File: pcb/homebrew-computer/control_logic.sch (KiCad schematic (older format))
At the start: 24 parts

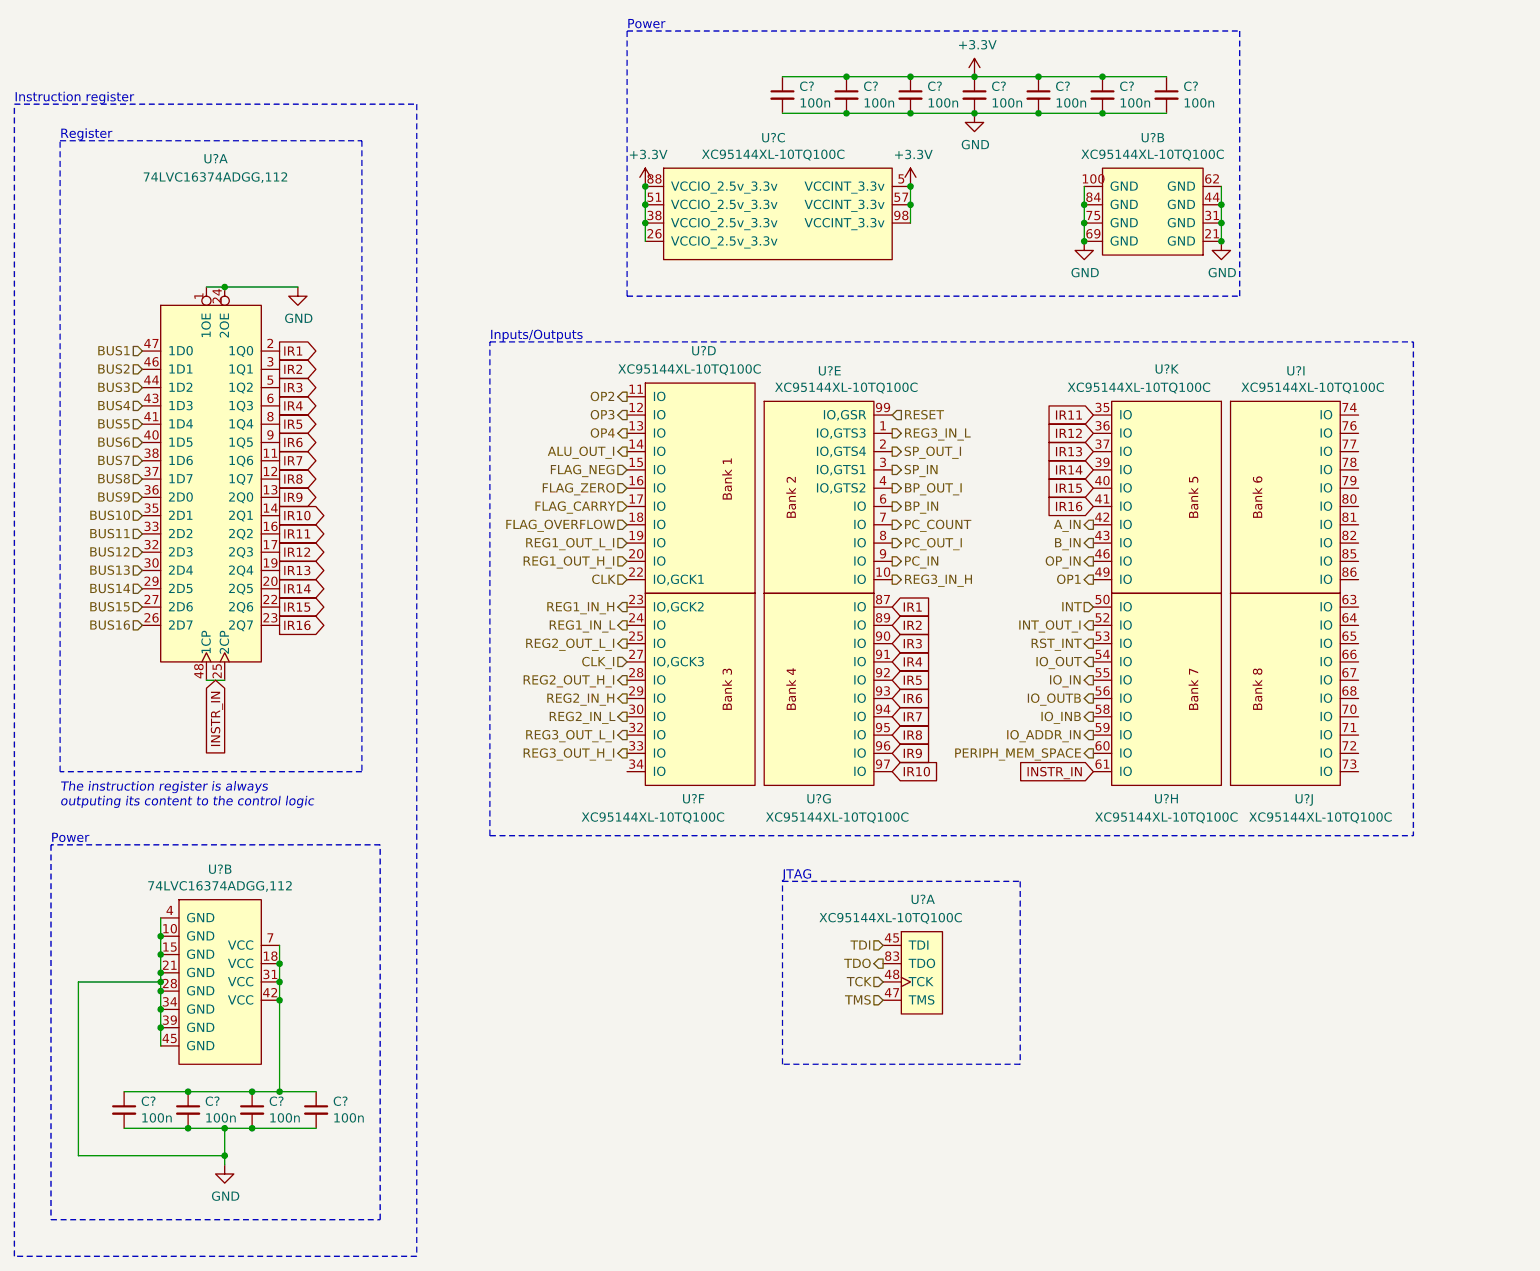
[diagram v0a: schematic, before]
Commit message: Start changing global labels with local labels
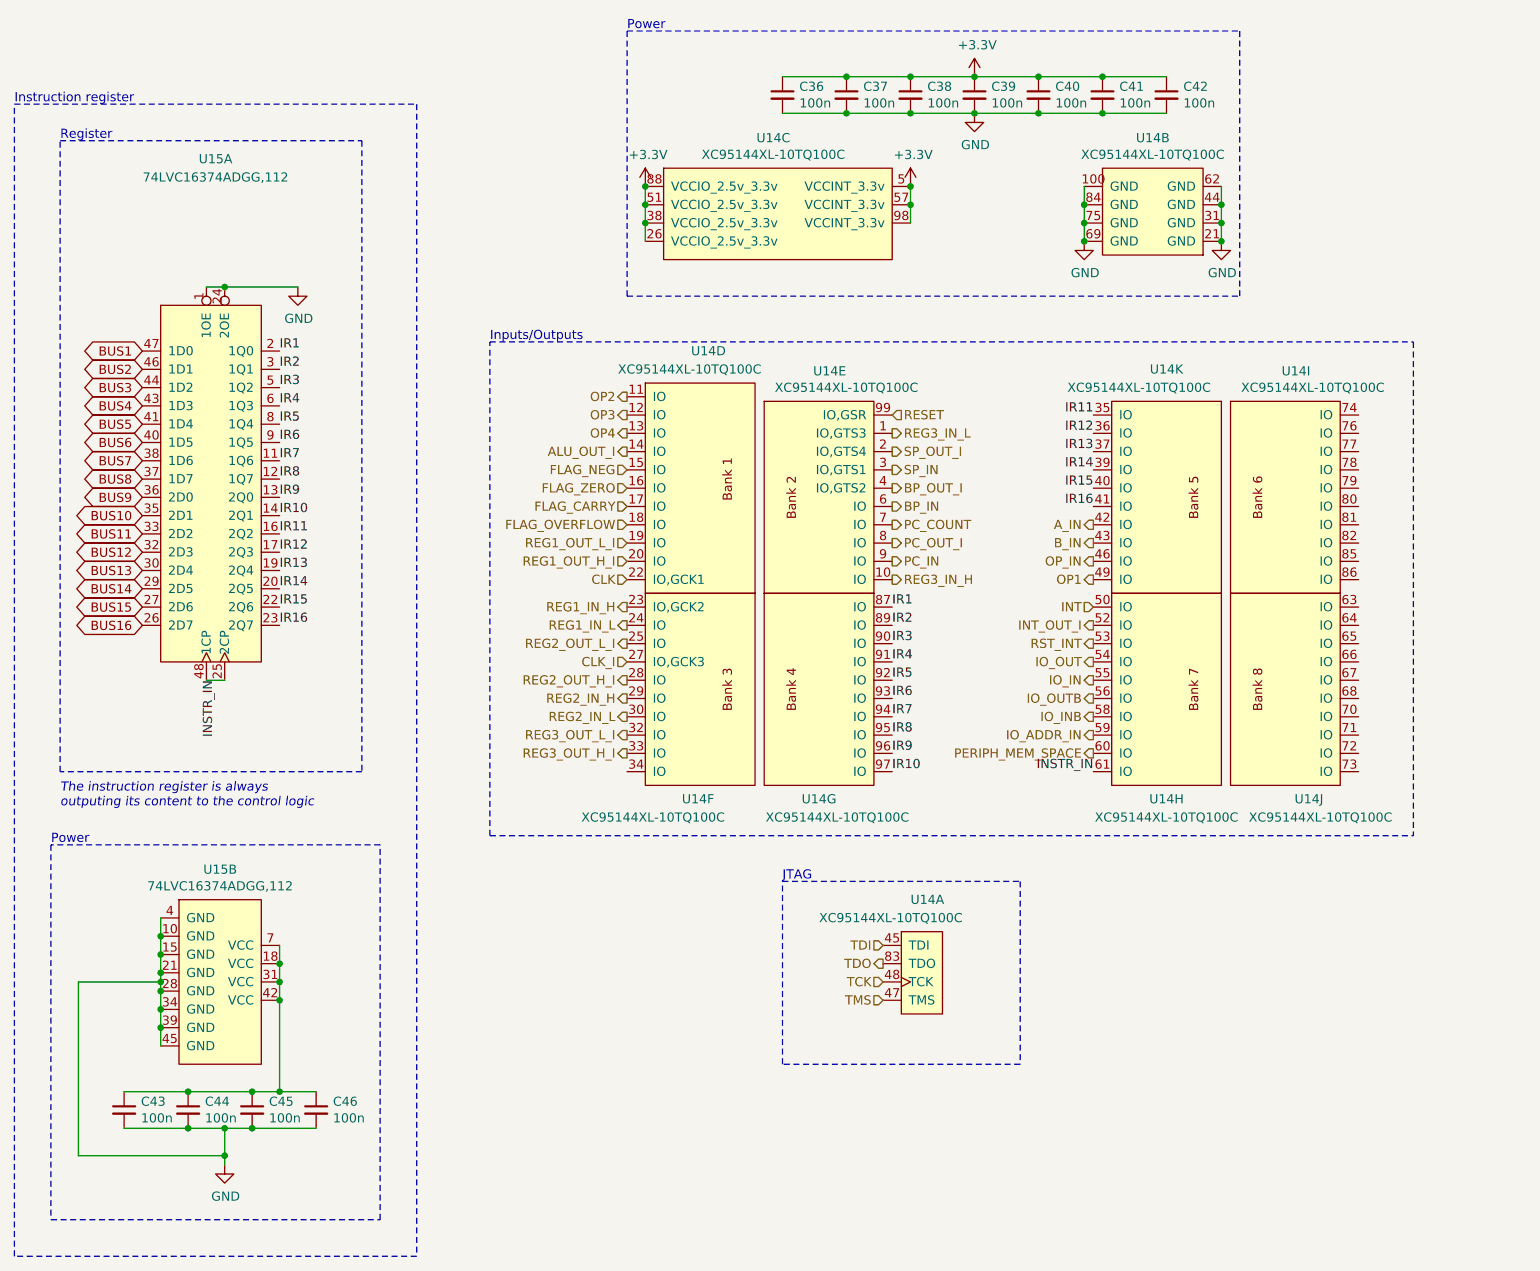
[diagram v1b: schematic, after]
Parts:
- gave numbers to parts that had none: 13

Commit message: Start working on the pcb layout
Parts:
- C36, C37, C38, C39, C40, C41, C42, C43, C44, C45, C46: footprint (none) -> Capacitor_SMD:C_0402_1005Metric_Pad0.74x0.62mm_HandSolder
- U14: footprint (none) -> Package_QFP:TQFP-100_14x14mm_P0.5mm
- U15: footprint (none) -> Package_SO:TSSOP-48_6.1x12.5mm_P0.5mm
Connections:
- net +3V3: now also C43.1, C44.1, C45.1, C46.1, U15.18 (VCC), U15.31 (VCC), U15.42 (VCC), U15.7 (VCC)
- no-connect marks 0 -> 21
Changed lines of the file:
@@
 F 0 "C39" H 6342 1046 50  0000 L CNN
 F 1 "100n" H 6342 955 50  0000 L CNN
-F 2 "" H 6250 1000 50  0001 C CNN
+F 2 "Capacitor_SMD:C_0402_1005Metric_Pad0.74x0.62mm_HandSolder" H 6250 1000 50  0001 C CNN
 F 3 "~" H 6250 1000 50  0001 C CNN
 	1    6250 1000
@@
 F 0 "C40" H 6692 1046 50  0000 L CNN
 F 1 "100n" H 6692 955 50  0000 L CNN
-F 2 "" H 6600 1000 50  0001 C CNN
+F 2 "Capacitor_SMD:C_0402_1005Metric_Pad0.74x0.62mm_HandSolder" H 6600 1000 50  0001 C CNN
 F 3 "~" H 6600 1000 50  0001 C CNN
 	1    6600 1000
@@
 F 0 "C41" H 7042 1046 50  0000 L CNN
 F 1 "100n" H 7042 955 50  0000 L CNN
-F 2 "" H 6950 1000 50  0001 C CNN
+F 2 "Capacitor_SMD:C_0402_1005Metric_Pad0.74x0.62mm_HandSolder" H 6950 1000 50  0001 C CNN
 F 3 "~" H 6950 1000 50  0001 C CNN
 	1    6950 1000
@@
 F 0 "U15" H 2100 2150 50  0000 C CNN
 F 1 "74LVC16374ADGG,112" H 2100 2050 50  0000 C CNN
-F 2 "" H 2100 1750 50  0001 C CNN
+F 2 "Package_SO:TSSOP-48_6.1x12.5mm_P0.5mm" H 2100 1750 50  0001 C CNN
 F 3 "" H 2100 1750 50  0001 C CNN
 	1    2100 1750
@@
 F 0 "U15" H 2125 5265 50  0000 C CNN
 F 1 "74LVC16374ADGG,112" H 2125 5174 50  0000 C CNN
-F 2 "" H 2100 5250 50  0001 C CNN
+F 2 "Package_SO:TSSOP-48_6.1x12.5mm_P0.5mm" H 2100 5250 50  0001 C CNN
 F 3 "" H 2100 5250 50  0001 C CNN
 	2    2100 5250
@@
 F 0 "C46" H 2742 6596 50  0000 L CNN
 F 1 "100n" H 2742 6505 50  0000 L CNN
-F 2 "" H 2650 6550 50  0001 C CNN
+F 2 "Capacitor_SMD:C_0402_1005Metric_Pad0.74x0.62mm_HandSolder" H 2650 6550 50  0001 C CNN
 F 3 "~" H 2650 6550 50  0001 C CNN
 	1    2650 6550
@@
 F 0 "C43" H 1692 6596 50  0000 L CNN
 F 1 "100n" H 1692 6505 50  0000 L CNN
-F 2 "" H 1600 6550 50  0001 C CNN
+F 2 "Capacitor_SMD:C_0402_1005Metric_Pad0.74x0.62mm_HandSolder" H 1600 6550 50  0001 C CNN
 F 3 "~" H 1600 6550 50  0001 C CNN
 	1    1600 6550
@@
 F 0 "C44" H 2042 6596 50  0000 L CNN
 F 1 "100n" H 2042 6505 50  0000 L CNN
-F 2 "" H 1950 6550 50  0001 C CNN
+F 2 "Capacitor_SMD:C_0402_1005Metric_Pad0.74x0.62mm_HandSolder" H 1950 6550 50  0001 C CNN
 F 3 "~" H 1950 6550 50  0001 C CNN
 	1    1950 6550
@@
 F 0 "C45" H 2392 6596 50  0000 L CNN
 F 1 "100n" H 2392 6505 50  0000 L CNN
-F 2 "" H 2300 6550 50  0001 C CNN
+F 2 "Capacitor_SMD:C_0402_1005Metric_Pad0.74x0.62mm_HandSolder" H 2300 6550 50  0001 C CNN
 F 3 "~" H 2300 6550 50  0001 C CNN
 	1    2300 6550
@@
 F 0 "U14" H 5900 5500 50  0000 L CNN
 F 1 "XC95144XL-10TQ100C" H 5400 5400 50  0000 L CNN
-F 2 "" H 5950 5450 50  0001 C CNN
+F 2 "Package_QFP:TQFP-100_14x14mm_P0.5mm" H 5950 5450 50  0001 C CNN
 F 3 "" H 5950 5450 50  0001 C CNN
 	1    5950 5450
@@
 F 0 "U14" H 7225 1365 50  0000 C CNN
 F 1 "XC95144XL-10TQ100C" H 7225 1274 50  0000 C CNN
-F 2 "" H 7200 1300 50  0001 C CNN
+F 2 "Package_QFP:TQFP-100_14x14mm_P0.5mm" H 7200 1300 50  0001 C CNN
 F 3 "" H 7200 1300 50  0001 C CNN
 	2    7200 1300
@@
 F 0 "U14" H 5150 1265 50  0000 C CNN
 F 1 "XC95144XL-10TQ100C" H 5150 1174 50  0000 C CNN
-F 2 "" H 5100 1250 50  0001 C CNN
+F 2 "Package_QFP:TQFP-100_14x14mm_P0.5mm" H 5100 1250 50  0001 C CNN
 F 3 "" H 5100 1250 50  0001 C CNN
 	3    5100 1250
@@
 F 0 "C36" H 5292 1046 50  0000 L CNN
 F 1 "100n" H 5292 955 50  0000 L CNN
-F 2 "" H 5200 1000 50  0001 C CNN
+F 2 "Capacitor_SMD:C_0402_1005Metric_Pad0.74x0.62mm_HandSolder" H 5200 1000 50  0001 C CNN
 F 3 "~" H 5200 1000 50  0001 C CNN
 	1    5200 1000
@@
 F 0 "C37" H 5642 1046 50  0000 L CNN
 F 1 "100n" H 5642 955 50  0000 L CNN
-F 2 "" H 5550 1000 50  0001 C CNN
+F 2 "Capacitor_SMD:C_0402_1005Metric_Pad0.74x0.62mm_HandSolder" H 5550 1000 50  0001 C CNN
 F 3 "~" H 5550 1000 50  0001 C CNN
 	1    5550 1000
@@
 F 0 "C38" H 5992 1046 50  0000 L CNN
 F 1 "100n" H 5992 955 50  0000 L CNN
-F 2 "" H 5900 1000 50  0001 C CNN
+F 2 "Capacitor_SMD:C_0402_1005Metric_Pad0.74x0.62mm_HandSolder" H 5900 1000 50  0001 C CNN
 F 3 "~" H 5900 1000 50  0001 C CNN
 	1    5900 1000
@@
 F 0 "C42" H 7392 1046 50  0000 L CNN
 F 1 "100n" H 7392 955 50  0000 L CNN
-F 2 "" H 7300 1000 50  0001 C CNN
+F 2 "Capacitor_SMD:C_0402_1005Metric_Pad0.74x0.62mm_HandSolder" H 7300 1000 50  0001 C CNN
 F 3 "~" H 7300 1000 50  0001 C CNN
 	1    7300 1000
@@
 F 0 "U14" H 4200 2400 50  0000 R CNN
 F 1 "XC95144XL-10TQ100C" H 4600 2300 50  0000 R CNN
-F 2 "" H 4450 2400 50  0001 C CNN
+F 2 "Package_QFP:TQFP-100_14x14mm_P0.5mm" H 4450 2400 50  0001 C CNN
 F 3 "" H 4450 2400 50  0001 C CNN
 	4    4450 2400
@@
 F 0 "U14" H 4650 2350 50  0000 R CNN
 F 1 "XC95144XL-10TQ100C" H 5200 2250 50  0000 R CNN
-F 2 "" H 4650 3600 50  0001 C CNN
+F 2 "Package_QFP:TQFP-100_14x14mm_P0.5mm" H 4650 3600 50  0001 C CNN
 F 3 "" H 4650 3600 50  0001 C CNN
 	6    4650 3600
@@
 F 0 "U14" H 7200 250 50  0000 C CNN
 F 1 "XC95144XL-10TQ100C" H 7200 150 50  0000 C CNN
-F 2 "" H 7250 2550 50  0001 C CNN
+F 2 "Package_QFP:TQFP-100_14x14mm_P0.5mm" H 7250 2550 50  0001 C CNN
 F 3 "" H 7250 2550 50  0001 C CNN
 	8    7250 2550
@@
 F 0 "U14" H 8008 2690 50  0000 C CNN
 F 1 "XC95144XL-10TQ100C" H 8100 2600 50  0000 C CNN
-F 2 "" H 7950 2575 50  0001 C CNN
+F 2 "Package_QFP:TQFP-100_14x14mm_P0.5mm" H 7950 2575 50  0001 C CNN
 F 3 "" H 7950 2575 50  0001 C CNN
 	9    7950 2600
@@
 F 0 "U14" H 6600 2350 50  0000 R CNN
 F 1 "XC95144XL-10TQ100C" H 6850 2250 50  0000 R CNN
-F 2 "" H 7300 3575 50  0001 C CNN
+F 2 "Package_QFP:TQFP-100_14x14mm_P0.5mm" H 7300 3575 50  0001 C CNN
 F 3 "" H 7300 3575 50  0001 C CNN
 	10   7300 3600
@@
 F 0 "U14" H 5458 2490 50  0000 C CNN
 F 1 "XC95144XL-10TQ100C" H 5550 2400 50  0000 C CNN
-F 2 "" H 5700 2475 50  0001 C CNN
+F 2 "Package_QFP:TQFP-100_14x14mm_P0.5mm" H 5700 2475 50  0001 C CNN
 F 3 "" H 5700 2475 50  0001 C CNN
 	5    5700 2500
@@
 F 0 "U14" H 5400 2350 50  0000 C CNN
 F 1 "XC95144XL-10TQ100C" H 5500 2250 50  0000 C CNN
-F 2 "" H 5500 3600 50  0001 C CNN
+F 2 "Package_QFP:TQFP-100_14x14mm_P0.5mm" H 5500 3600 50  0001 C CNN
 F 3 "" H 5500 3600 50  0001 C CNN
 	7    5500 3600
@@
 F 0 "U14" H 7300 4700 50  0000 C CNN
 F 1 "XC95144XL-10TQ100C" H 7150 4600 50  0000 C CNN
-F 2 "" H 7950 3575 50  0001 C CNN
+F 2 "Package_QFP:TQFP-100_14x14mm_P0.5mm" H 7950 3575 50  0001 C CNN
 F 3 "" H 7950 3575 50  0001 C CNN
 	11   7950 3600
@@
 Text Label 2100 4200 3    50   ~ 0
 INSTR_IN
+NoConn ~ 4350 4700
+NoConn ~ 8350 2750
+NoConn ~ 8350 2850
+NoConn ~ 8350 2950
+NoConn ~ 8350 3050
+NoConn ~ 8350 3150
+NoConn ~ 8350 3250
+NoConn ~ 8350 3350
+NoConn ~ 8350 3450
+NoConn ~ 8350 3550
+NoConn ~ 8350 3650
+NoConn ~ 8350 3800
+NoConn ~ 8350 3900
+NoConn ~ 8350 4000
+NoConn ~ 8350 4100
+NoConn ~ 8350 4200
+NoConn ~ 8350 4300
+NoConn ~ 8350 4400
+NoConn ~ 8350 4500
+NoConn ~ 8350 4600
+NoConn ~ 8350 4700
+$Comp
+L power:+3.3V #PWR?
+U 1 1 5FA740EC
+P 2450 5650
+AR Path="/5F8B5CB7/5FA740EC" Ref="#PWR?"  Part="1"
+AR Path="/5F95DC76/5FA740EC" Ref="#PWR?"  Part="1"
+AR Path="/5F8B5E3D/5FA740EC" Ref="#PWR0166"  Part="1"
+F 0 "#PWR0166" H 2450 5500 50  0001 C CNN
+F 1 "+3.3V" H 2600 5700 50  0000 C CNN
+F 2 "" H 2450 5650 50  0001 C CNN
+F 3 "" H 2450 5650 50  0001 C CNN
+	1    2450 5650
+	1    0    0    -1
+$EndComp
+Connection ~ 2450 5650
 $EndSCHEMATC

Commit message: Keep working on the layout
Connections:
- net A_IN: now also U14.89 (IO); no longer U14.42 (IO)
- net BP_IN: now also U14.32 (IO); no longer U14.6 (IO)
- net BP_OUT_I: now also U14.30 (IO); no longer U14.4 (IO,GTS2)
- net B_IN: now also U14.87 (IO); no longer U14.43 (IO)
- net FLAG_CARRY: now also U14.78 (IO); no longer U14.17 (IO)
- net FLAG_NEG: now also U14.77 (IO); no longer U14.15 (IO)
- net FLAG_OVERFLOW: now also U14.79 (IO); no longer U14.18 (IO)
- net FLAG_ZERO: now also U14.76 (IO); no longer U14.16 (IO)
- net INSTR_IN: now also U14.97 (IO); no longer U14.61 (IO)
- net IR1: now also U14.90 (IO); no longer U14.87 (IO)
- net IR10: now also U14.3 (IO,GTS1); no longer U14.97 (IO)
- net IR11: now also U14.4 (IO,GTS2); no longer U14.35 (IO)
- net IR12: now also U14.6 (IO); no longer U14.36 (IO)
- net IR13: now also U14.7 (IO); no longer U14.37 (IO)
- net IR14: now also U14.8 (IO); no longer U14.39 (IO)
- net IR15: now also U14.9 (IO); no longer U14.40 (IO)
- net IR16: now also U14.10 (IO); no longer U14.41 (IO)
- net IR2: now also U14.91 (IO); no longer U14.89 (IO)
- net IR3: now also U14.92 (IO); no longer U14.90 (IO)
- net IR4: now also U14.93 (IO); no longer U14.91 (IO)
- net IR5: now also U14.94 (IO); no longer U14.92 (IO)
- net IR6: now also U14.95 (IO); no longer U14.93 (IO)
- net IR7: now also U14.96 (IO); no longer U14.94 (IO)
- net IR8: now also U14.1 (IO,GTS3); no longer U14.95 (IO)
- net IR9: now also U14.2 (IO,GTS4); no longer U14.96 (IO)
- net OP1: now also U14.86 (IO); no longer U14.49 (IO)
- net OP2: now also U14.85 (IO); no longer U14.11 (IO)
- net OP3: now also U14.82 (IO); no longer U14.12 (IO)
- net OP4: now also U14.81 (IO); no longer U14.13 (IO)
- net OP_IN: now also U14.80 (IO); no longer U14.46 (IO)
- net PC_COUNT: now also U14.73 (IO); no longer U14.7 (IO)
- net PC_IN: now also U14.72 (IO); no longer U14.9 (IO)
- net PC_OUT_I: now also U14.74 (IO); no longer U14.8 (IO)
- net REG1_IN_H: now also U14.29 (IO); no longer U14.23 (IO,GCK2)
- net REG1_IN_L: no longer U14.24 (IO)
- net REG1_OUT_H_I: no longer U14.20 (IO)
- net REG1_OUT_L_I: no longer U14.19 (IO)
- net REG2_IN_H: no longer U14.29 (IO)
- net REG2_IN_L: no longer U14.30 (IO)
- net REG2_OUT_L_I: no longer U14.25 (IO)
- net REG3_IN_H: now also U14.41 (IO); no longer U14.10 (IO)
- net REG3_IN_L: now also U14.11 (IO); no longer U14.1 (IO,GTS3)
- net REG3_OUT_H_I: no longer U14.33 (IO)
- net REG3_OUT_L_I: no longer U14.32 (IO)
- net SP_IN: now also U14.34 (IO); no longer U14.3 (IO,GTS1)
- net SP_OUT_I: now also U14.33 (IO); no longer U14.2 (IO,GTS4)
- no-connect marks 21 -> 8
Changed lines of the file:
@@
 Wire Wire Line
 	2050 4200 2150 4200
-Text HLabel 6900 3350 0    50   Output ~ 0
+Text HLabel 5800 3900 2    50   Output ~ 0
 A_IN
-Text HLabel 6900 3450 0    50   Output ~ 0
+Text HLabel 5800 3800 2    50   Output ~ 0
 B_IN
-Text HLabel 6900 3550 0    50   Output ~ 0
+Text HLabel 8350 3250 2    50   Output ~ 0
 OP_IN
-Text HLabel 6900 3650 0    50   Output ~ 0
+Text HLabel 8350 3650 2    50   Output ~ 0
 OP1
-Text HLabel 4350 2650 0    50   Output ~ 0
+Text HLabel 8350 3550 2    50   Output ~ 0
 OP2
-Text HLabel 4350 2750 0    50   Output ~ 0
+Text HLabel 8350 3450 2    50   Output ~ 0
 OP3
-Text HLabel 4350 2850 0    50   Output ~ 0
+Text HLabel 8350 3350 2    50   Output ~ 0
 OP4
 Text HLabel 4350 2950 0    50   Output ~ 0
 ALU_OUT_I
-Text HLabel 4350 3050 0    50   Input ~ 0
+Text HLabel 8350 2950 2    50   Input ~ 0
 FLAG_NEG
-Text HLabel 4350 3150 0    50   Input ~ 0
+Text HLabel 8350 2850 2    50   Input ~ 0
 FLAG_ZERO
-Text HLabel 4350 3250 0    50   Input ~ 0
+Text HLabel 8350 3050 2    50   Input ~ 0
 FLAG_CARRY
-Text HLabel 4350 3350 0    50   Input ~ 0
+Text HLabel 8350 3150 2    50   Input ~ 0
 FLAG_OVERFLOW
-Text HLabel 4350 3450 0    50   Input ~ 0
+Text HLabel 4100 3500 0    50   Input ~ 0
 REG1_OUT_L_I
-Text HLabel 4350 3550 0    50   Input ~ 0
+Text HLabel 4100 3200 0    50   Input ~ 0
 REG1_OUT_H_I
-Text HLabel 4350 3800 0    50   Output ~ 0
+Text HLabel 4350 4300 0    50   Output ~ 0
 REG1_IN_H
-Text HLabel 4350 3900 0    50   Output ~ 0
+Text HLabel 4100 3300 0    50   Output ~ 0
 REG1_IN_L
-Text HLabel 4350 4000 0    50   Output ~ 0
+Text HLabel 4100 3400 0    50   Output ~ 0
 REG2_OUT_L_I
 Text HLabel 4350 4200 0    50   Output ~ 0
 REG2_OUT_H_I
-Text HLabel 4350 4300 0    50   Output ~ 0
+Text HLabel 4100 3700 0    50   Output ~ 0
 REG2_IN_H
+Text HLabel 4100 3800 0    50   Output ~ 0
+REG2_IN_L
+Text HLabel 4100 3900 0    50   Output ~ 0
+REG3_OUT_L_I
+Text HLabel 4100 4000 0    50   Output ~ 0
+REG3_OUT_H_I
+Text HLabel 6900 3250 0    50   Output ~ 0
+REG3_IN_H
+Text HLabel 4350 2650 0    50   Output ~ 0
+REG3_IN_L
+Text HLabel 4350 4600 0    50   Output ~ 0
+SP_OUT_I
+Text HLabel 4350 4700 0    50   Output ~ 0
+SP_IN
 Text HLabel 4350 4400 0    50   Output ~ 0
-REG2_IN_L
+BP_OUT_I
 Text HLabel 4350 4500 0    50   Output ~ 0
-REG3_OUT_L_I
-Text HLabel 4350 4600 0    50   Output ~ 0
-REG3_OUT_H_I
-Text HLabel 5800 3650 2    50   Output ~ 0
-REG3_IN_H
-Text HLabel 5800 2850 2    50   Output ~ 0
-REG3_IN_L
-Text HLabel 5800 2950 2    50   Output ~ 0
-SP_OUT_I
-Text HLabel 5800 3050 2    50   Output ~ 0
-SP_IN
-Text HLabel 5800 3150 2    50   Output ~ 0
-BP_OUT_I
-Text HLabel 5800 3250 2    50   Output ~ 0
 BP_IN
-Text HLabel 5800 3350 2    50   Output ~ 0
+Text HLabel 8350 4700 2    50   Output ~ 0
 PC_COUNT
-Text HLabel 5800 3450 2    50   Output ~ 0
+Text HLabel 8350 2750 2    50   Output ~ 0
 PC_OUT_I
-Text HLabel 5800 3550 2    50   Output ~ 0
+Text HLabel 8350 4600 2    50   Output ~ 0
 PC_IN
 $Comp
@@
 Text Label 2450 3900 0    50   ~ 0
 IR16
-Text Label 5800 3800 0    50   ~ 0
+Text Label 5800 4000 0    50   ~ 0
 IR1
-Text Label 5800 3900 0    50   ~ 0
+Text Label 5800 4100 0    50   ~ 0
 IR2
-Text Label 5800 4000 0    50   ~ 0
+Text Label 5800 4200 0    50   ~ 0
 IR3
-Text Label 5800 4100 0    50   ~ 0
+Text Label 5800 4300 0    50   ~ 0
 IR4
-Text Label 5800 4200 0    50   ~ 0
+Text Label 5800 4400 0    50   ~ 0
 IR5
-Text Label 5800 4300 0    50   ~ 0
+Text Label 5800 4500 0    50   ~ 0
 IR6
-Text Label 5800 4400 0    50   ~ 0
+Text Label 5800 4600 0    50   ~ 0
 IR7
-Text Label 5800 4500 0    50   ~ 0
+Text Label 5800 2850 0    50   ~ 0
 IR8
-Text Label 5800 4600 0    50   ~ 0
+Text Label 5800 2950 0    50   ~ 0
 IR9
+Text Label 5800 3050 0    50   ~ 0
+IR10
+Text Label 5800 3150 0    50   ~ 0
+IR11
+Text Label 5800 3250 0    50   ~ 0
+IR12
+Text Label 5800 3350 0    50   ~ 0
+IR13
+Text Label 5800 3450 0    50   ~ 0
+IR14
+Text Label 5800 3550 0    50   ~ 0
+IR15
+Text Label 5800 3650 0    50   ~ 0
+IR16
 Text Label 5800 4700 0    50   ~ 0
-IR10
-Text Label 6900 2750 2    50   ~ 0
-IR11
-Text Label 6900 2850 2    50   ~ 0
-IR12
-Text Label 6900 2950 2    50   ~ 0
-IR13
-Text Label 6900 3050 2    50   ~ 0
-IR14
-Text Label 6900 3150 2    50   ~ 0
-IR15
-Text Label 6900 3250 2    50   ~ 0
-IR16
-Text Label 6900 4700 2    50   ~ 0
 INSTR_IN
 Text Label 2100 4200 3    50   ~ 0
 INSTR_IN
-NoConn ~ 4350 4700
-NoConn ~ 8350 2750
-NoConn ~ 8350 2850
-NoConn ~ 8350 2950
-NoConn ~ 8350 3050
-NoConn ~ 8350 3150
-NoConn ~ 8350 3250
-NoConn ~ 8350 3350
-NoConn ~ 8350 3450
-NoConn ~ 8350 3550
-NoConn ~ 8350 3650
 NoConn ~ 8350 3800
 NoConn ~ 8350 3900
@@
 NoConn ~ 8350 4400
 NoConn ~ 8350 4500
-NoConn ~ 8350 4600
-NoConn ~ 8350 4700
 $Comp
 L power:+3.3V #PWR?
